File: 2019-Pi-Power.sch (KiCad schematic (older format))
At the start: 25 parts, among them J1 Barrel_Jack_Switch, J2 USB_A, J3 USB_A, J4 Conn_02x04_Odd_Even, J5 Conn_01x04, J6 Conn_01x04, J7 Conn_01x04, J8 Conn_02x02_Odd_Even, P1 Conn_02x20_Odd_Even, U1 MP1584

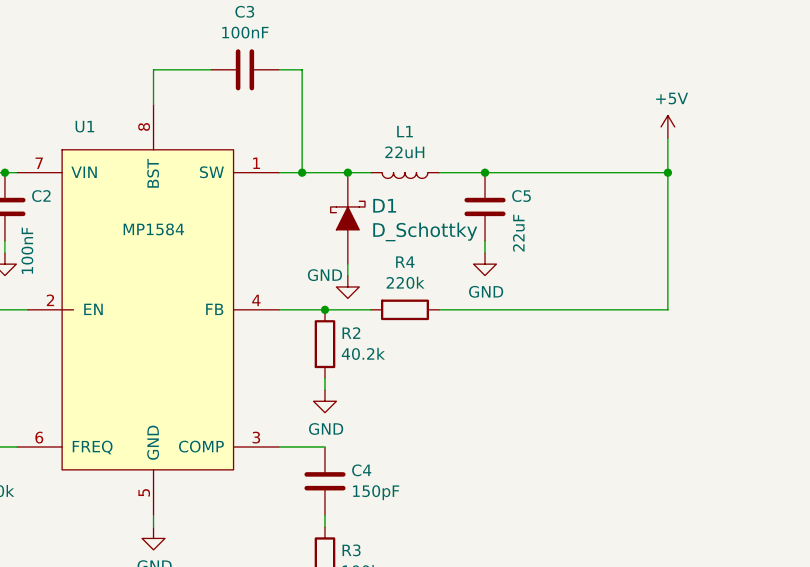
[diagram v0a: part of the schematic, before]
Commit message: labelling and component update
go from 220k to 210k, when powering over GPIO 5.2V is unecessary, going to 5.1V
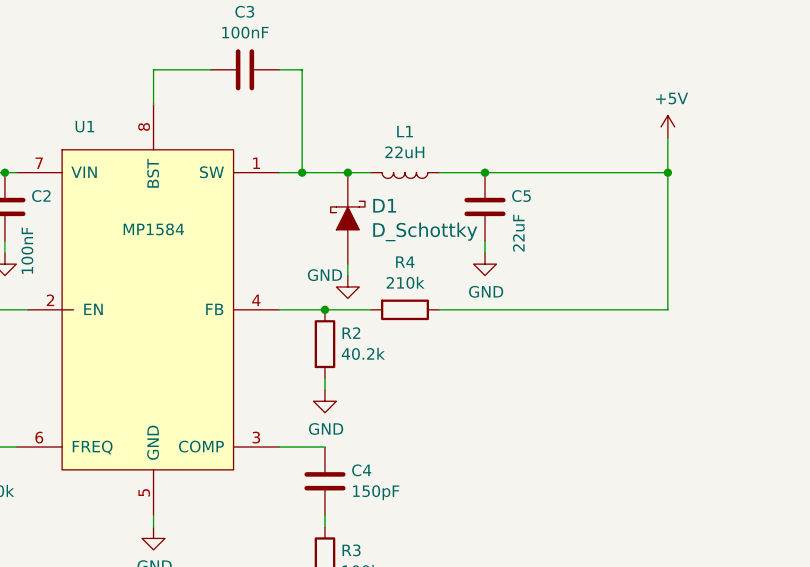
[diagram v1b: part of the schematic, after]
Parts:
- R4: value 220k -> 210k
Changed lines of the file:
@@
 P 4100 1900
 F 0 "R4" V 3893 1900 50  0000 C CNN
-F 1 "220k" V 3984 1900 50  0000 C CNN
+F 1 "210k" V 3984 1900 50  0000 C CNN
 F 2 "Resistors_SMD:R_0603" V 4030 1900 50  0001 C CNN
 F 3 "~" H 4100 1900 50  0001 C CNN
